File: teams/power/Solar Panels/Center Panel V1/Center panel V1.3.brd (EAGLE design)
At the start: 82 x 277.8 mm, 7 parts

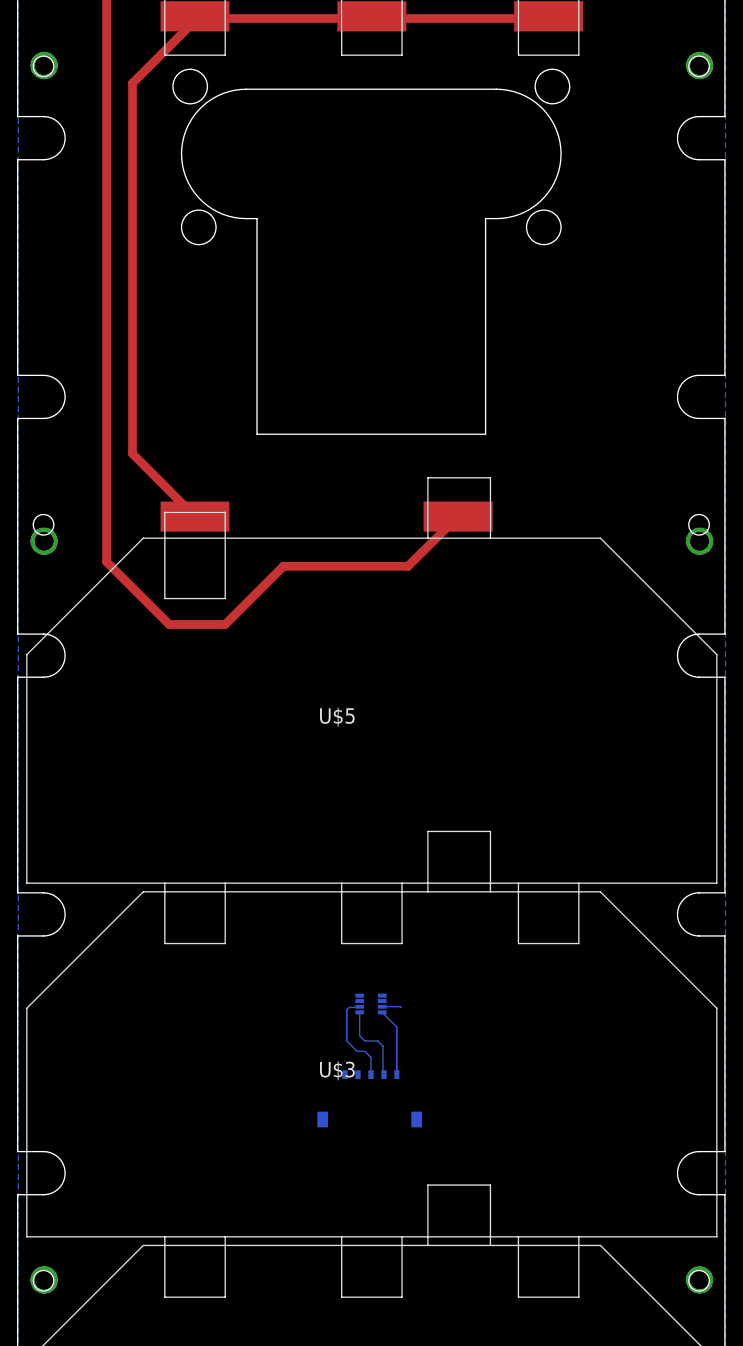
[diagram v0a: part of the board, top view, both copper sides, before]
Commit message: Changes to Center Panel V1.2, Tracking V1.3, and gerbers of V1.3
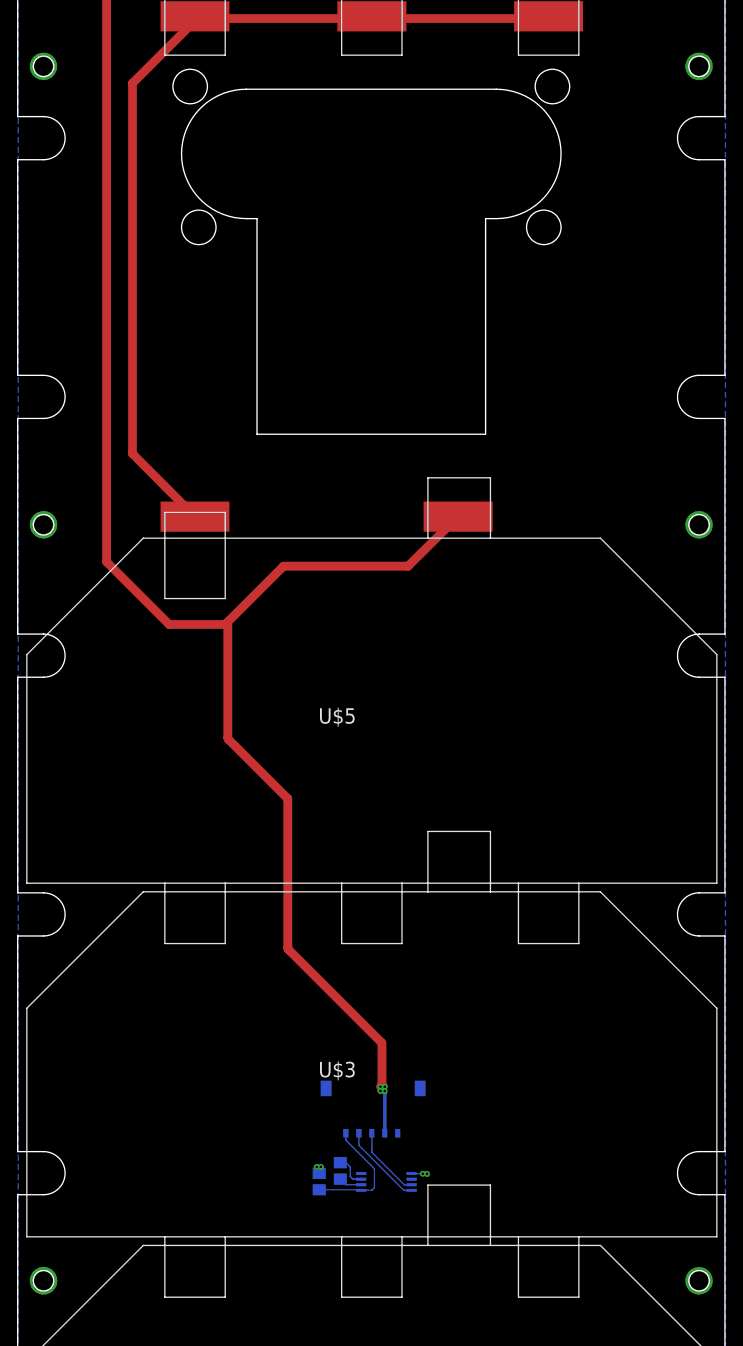
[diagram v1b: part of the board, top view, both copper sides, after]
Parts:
- removed U$4: INA219, DubSat1 Components:S008
- added C7: 100pF, Battery board V4.1 - simple signals:R0805
- added C8: (no value), Battery board V4.1 - simple signals:C0805
- added U$10: TMP411, DubSat1 Components:TSSOP-8
- moved U$7 9.13 mm to (44.0, 100.0), turned to 0 degrees
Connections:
- removed net N$8: U$5.P$1, U$6.P$5
- new net N$14: C7.1, U$10.2
- new net N$15: C7.2, U$10.3
- net GND: now also C8.2, U$10.5; no longer U$4.3
- net POWER: now also U$5.P$1, U$6.P$5
- net SCL: now also U$10.8; no longer U$4.5
- net SDA: now also U$10.7; no longer U$4.6
- net VS: now also C8.1, U$10.1; no longer U$4.4
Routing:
- net POWER: track 0.00 -> 230.1 mm, vias 0 -> 4
- net N$8: track 162.2 -> 0.00 mm
- net VS: track 7.93 -> 14.2 mm
- net N$15: track 0.00 -> 3.86 mm
- net N$14: track 0.00 -> 2.69 mm
- net SDA: track 10.8 -> 8.40 mm
- net GND: track 51.9 -> 51.5 mm, vias 4 -> 8
